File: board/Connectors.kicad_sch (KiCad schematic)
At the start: 20 parts, among them J10 SLOT 4, J11 SLOT 1, J12 SLOT 5, J13 SLOT 2, J14 SPI Device 0, J15 SPI Device 4, J16 SPI Device 1, J17 SPI Device 5, J19 SPI Device 2, J20 SPI Device 6, J21 SPI Device 3, J22 SPI Device 7, J23 SLOT 3, J24 VIA Port A, J25 SP720APP, J9 SLOT 0

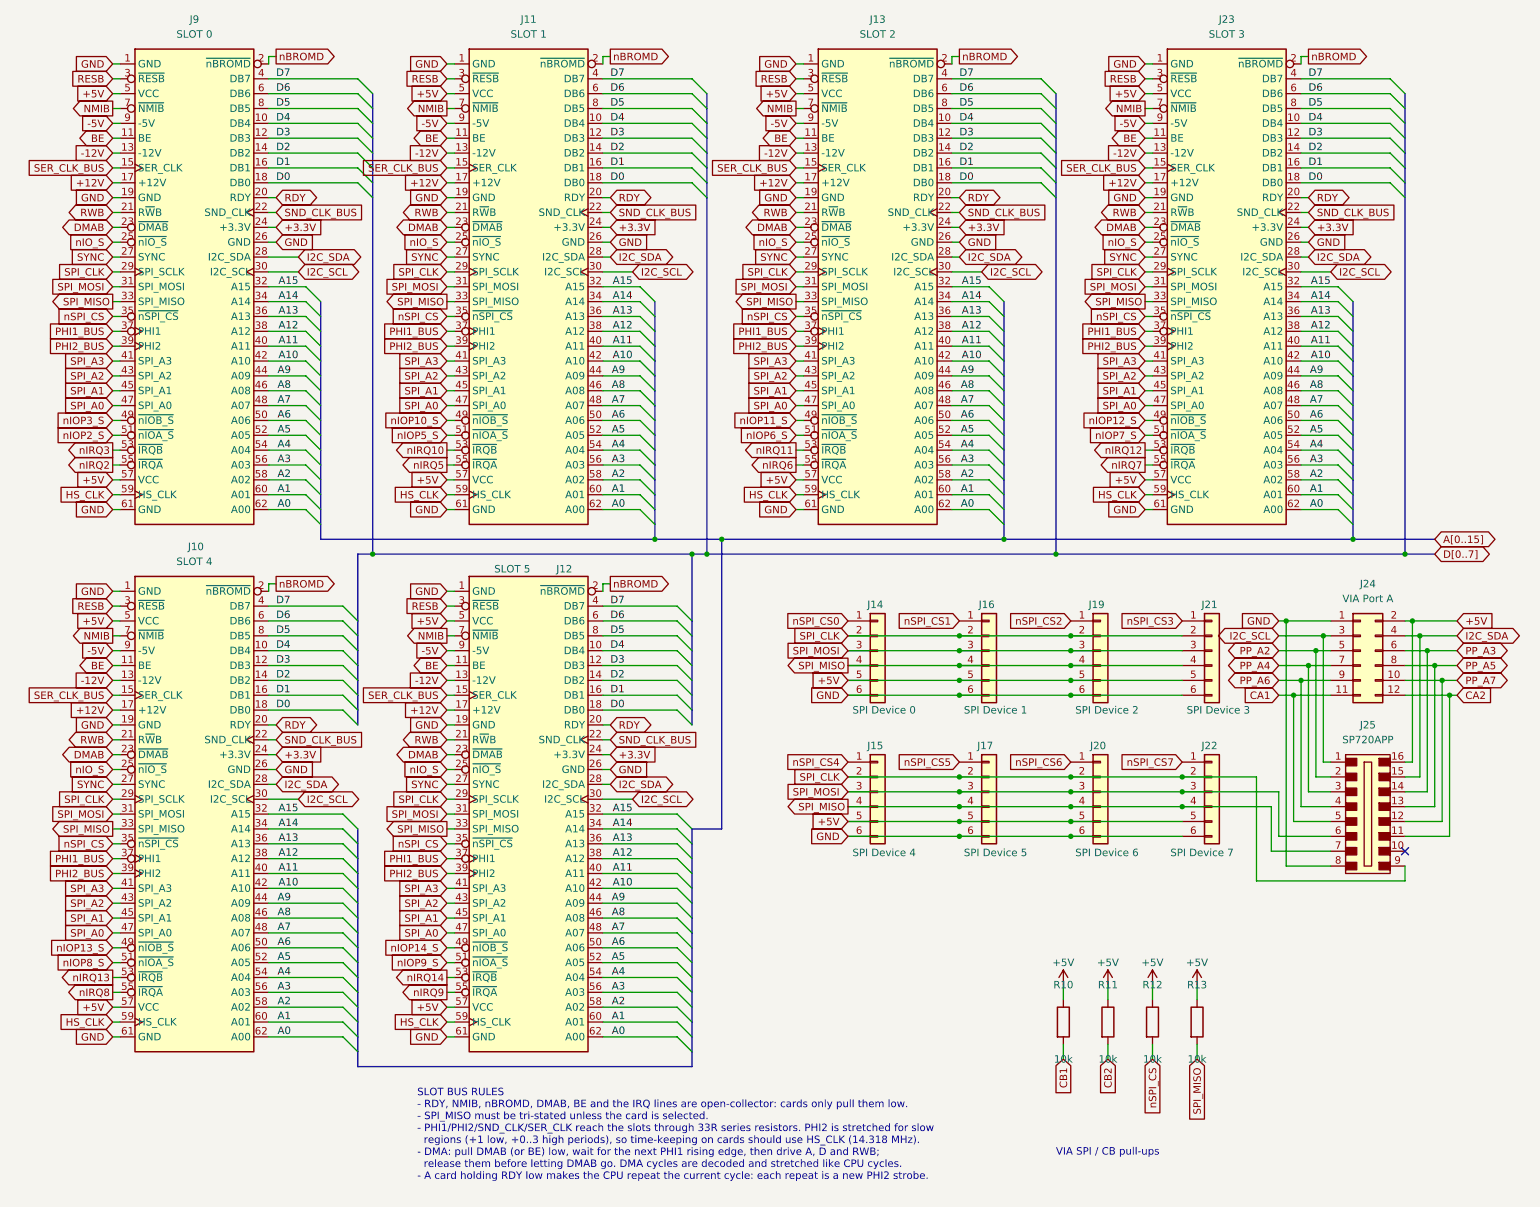
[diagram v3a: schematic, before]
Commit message: V2.0: slot pin 9 to +3.3V, amplifier on +5V
Slots:
- Pin 9 on all six slots now carries +3.3V instead of -5V, so each card
  gets two 3.3 V pins (9 and 24); no existing card used -5V
- Slot connector symbol pin 9 renamed +3.3V; slot bus rules note updated
- Removed U80 (79L05), C98 and C99 from the Power sheet

Amplifier:
- U89 TDA2822M now runs from +5V through an RC filter (R32 1R, C122 1000u)
- Removed U90 (L7809), C124 and C125
- R26/R27 470k (same volume range at 5 V); R30/R31 2.2R (same footprint)
- PWR_FLAG on the new AMP_5V net; sheet note updated

PCB updated from the schematic.

Also tidied overlapping text on the Power sheet (U78/U79 labels, PWR_FLAG,
R19/C111/R20/C112); connectivity unchanged.

Co-Authored-By: Claude Opus 5.5 <noreply@anthropic.com>
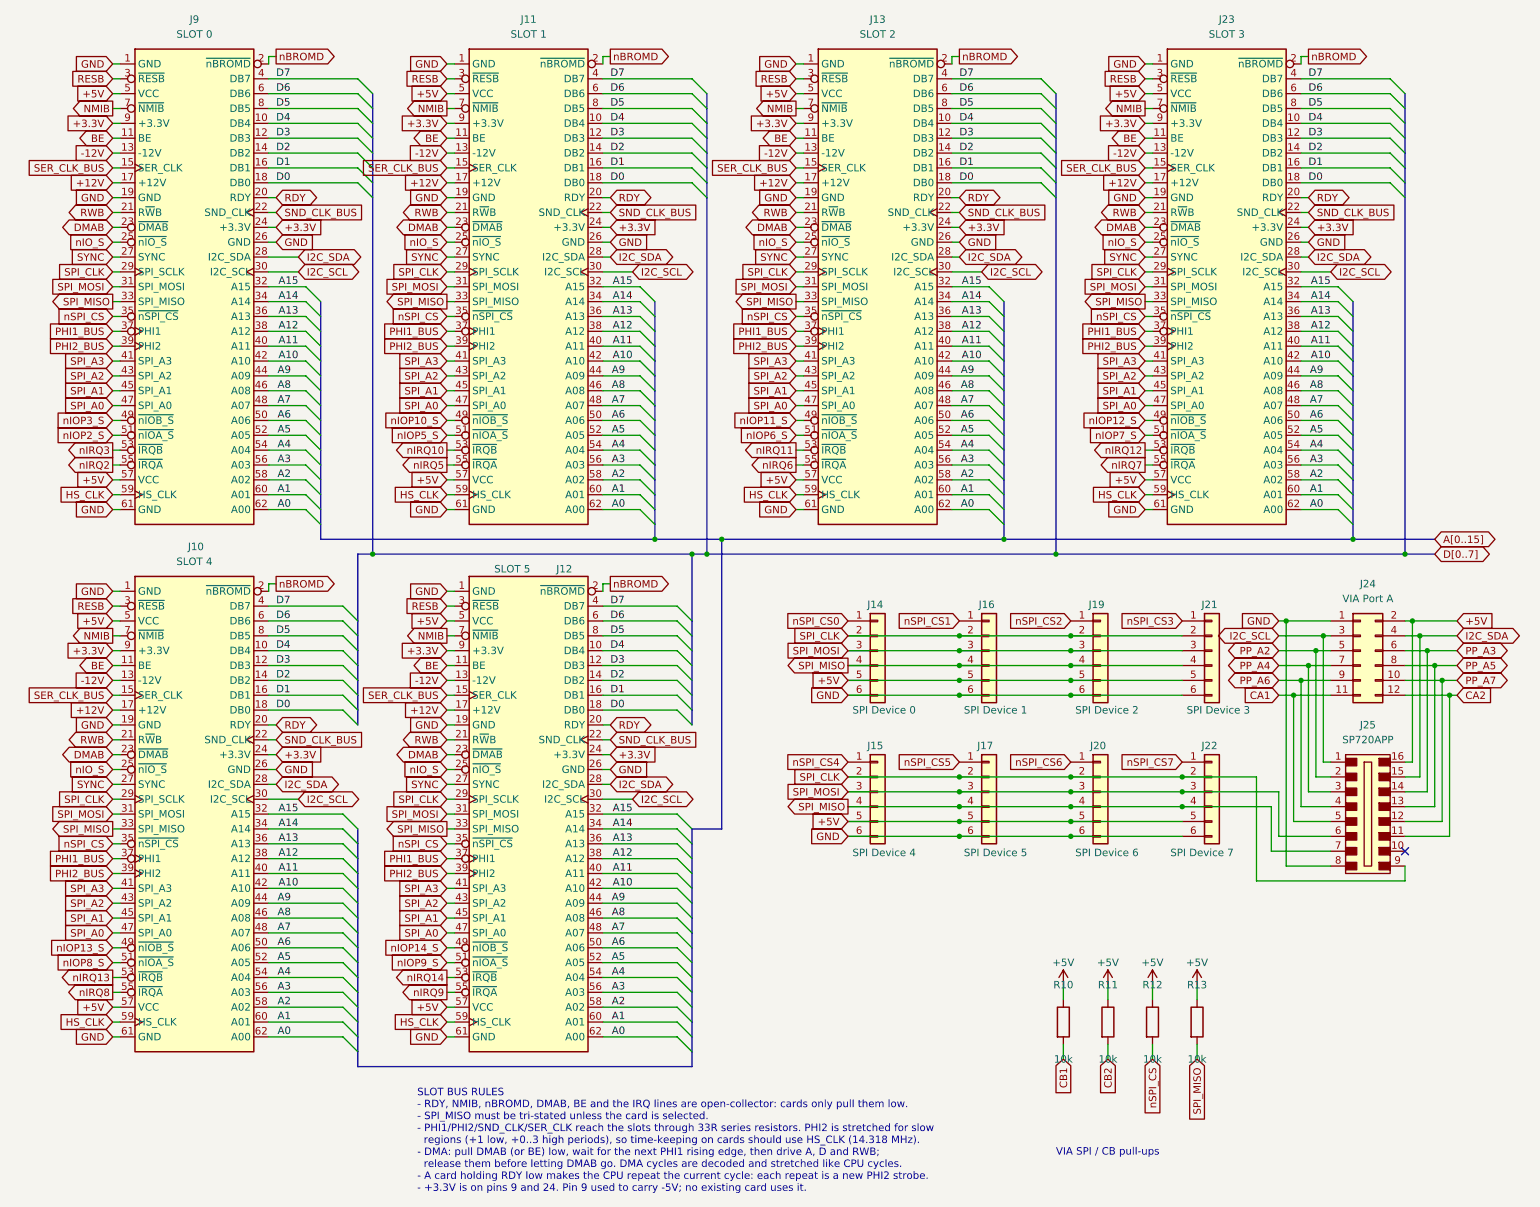
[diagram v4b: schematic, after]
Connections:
- net -5V is gone; now on net +3.3V: J10.9 (+3.3V), J11.9 (+3.3V), J12.9 (+3.3V), J13.9 (+3.3V), J23.9 (+3.3V), J9.9 (+3.3V)
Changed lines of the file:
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@@
 		(comment 1 "Hydra 16")
 	)
-	(text "SLOT BUS RULES\n- RDY, NMIB, nBROMD, DMAB, BE and the IRQ lines are open-collector: cards only pull them low.\n- SPI_MISO must be tri-stated unless the card is selected.\n- PHI1/PHI2/SND_CLK/SER_CLK reach the slots through 33R series resistors. PHI2 is stretched for slow\n  regions (+1 low, +0..3 high periods), so time-keeping on cards should use HS_CLK (14.318 MHz).\n- DMA: pull DMAB (or BE) low, wait for the next PHI1 rising edge, then drive A, D and RWB;\n  release them before letting DMAB go. DMA cycles are decoded and stretched like CPU cycles.\n- A card holding RDY low makes the CPU repeat the current cycle: each repeat is a new PHI2 strobe."
+	(text "SLOT BUS RULES\n- RDY, NMIB, nBROMD, DMAB, BE and the IRQ lines are open-collector: cards only pull them low.\n- SPI_MISO must be tri-stated unless the card is selected.\n- PHI1/PHI2/SND_CLK/SER_CLK reach the slots through 33R series resistors. PHI2 is stretched for slow\n  regions (+1 low, +0..3 high periods), so time-keeping on cards should use HS_CLK (14.318 MHz).\n- DMA: pull DMAB (or BE) low, wait for the next PHI1 rising edge, then drive A, D and RWB;\n  release them before letting DMAB go. DMA cycles are decoded and stretched like CPU cycles.\n- A card holding RDY low makes the CPU repeat the current cycle: each repeat is a new PHI2 strobe.\n- +3.3V is on pins 9 and 24. Pin 9 used to carry -5V; no existing card uses it."
 		(exclude_from_sim no)
 		(at 78.74 198.12 0)
@@
 		)
 	)
-	(global_label "-5V"
+	(global_label "+3.3V"
 		(shape input)
 		(at 143.51 33.02 180)
@@
 		)
 	)
-	(global_label "-5V"
+	(global_label "+3.3V"
 		(shape input)
 		(at 83.82 33.02 180)
@@
 		)
 	)
-	(global_label "-5V"
+	(global_label "+3.3V"
 		(shape input)
 		(at 26.67 123.19 180)
@@
 		)
 	)
-	(global_label "-5V"
+	(global_label "+3.3V"
 		(shape input)
 		(at 83.82 123.19 180)
@@
 		)
 	)
-	(global_label "-5V"
+	(global_label "+3.3V"
 		(shape input)
 		(at 26.67 33.02 180)
@@
 		)
 	)
-	(global_label "-5V"
+	(global_label "+3.3V"
 		(shape input)
 		(at 203.2 33.02 180)

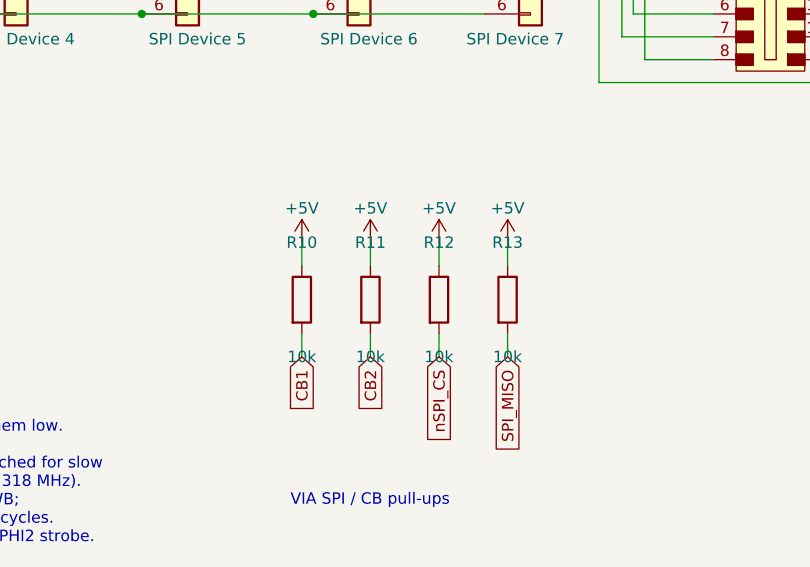
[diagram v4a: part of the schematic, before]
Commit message: V2.0: consolidate parts (239 -> 216), GAL C rev 02
No change in function:
- U9 74F08 removed: GAL C (U88) rev 02 makes the CPU phi0 (P_PHI0 = PHI2
  held low while DMAB_S is low); its decoupling cap C14 removed
- U34 74ACT14 removed: the two clock buffers use spare U19 74F240 gates
- U60 + U61 (2 x CY7C192 vector RAM) replaced by one AS7C256B-15
  (32K x 8, 15 ns); the IRQ sheet's D[0..7] bus is gone
- Crystal oscillators (U75 74HCU04, Y1, Y2, R1, R6-R8, C43, C44, C96,
  C97) replaced by canned oscillators X1 (14.31818 MHz), X2 (1.8432 MHz)
- Soft power: CD40106 -> 74HC14, CD4013 -> 74HC74 (active-low set/reset,
  power-on reset network inverted); a spare 74HC14 gate drives PS_ON#,
  so Q1 is removed
- R10-R13 -> RN6 (4 x 10k, SIP-5); R9, R21-R24 -> RN7 (5 x 33R isolated,
  SIP-10)
- C100-C102 (3 x 220u) -> C100 680u
- Clocks and Power sheet notes updated; PLD README updated

GAL C rev 02 verified against rev 01 over 200,000 clock edges.
PCB updated from the schematic (adds RN6, RN7, X1, X2 and the speakers
LS1/LS2). Also includes KiCad's re-save of the schematic sheets.

Co-Authored-By: Claude Opus 5.5 <noreply@anthropic.com>
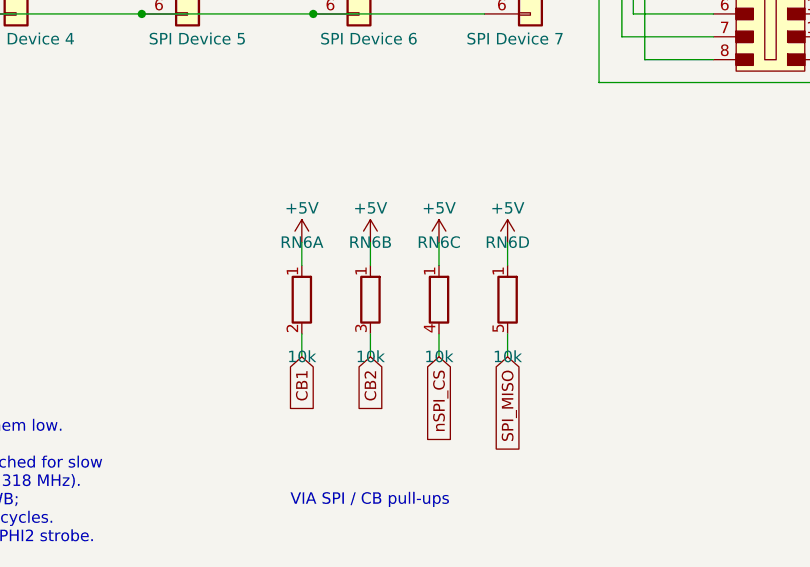
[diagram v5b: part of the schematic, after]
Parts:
- removed R11, R12, R13: 10k, Resistor_THT:R_Axial_DIN0204_L3.6mm_D1.6mm_P5.08mm_Horizontal, symbol Device:R
- added unit 2 of RN6
- added unit 3 of RN6
- added unit 4 of RN6
- RN6: renamed from R10; footprint Resistor_THT:R_Axial_DIN0204_L3.6mm_D1.6mm_P5.08mm_Horizontal -> Resistor_THT:R_Array_SIP5; symbol Device:R -> Device:R_Network04_Split
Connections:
- net +5V: now also RN6.1 (R1), RN6.1 (R1), RN6.1 (R1)
- net CB2: now also RN6.3 (R2.2)
- net SPI_MISO: now also RN6.5 (R4.2)
- net nSPI_CS: now also RN6.4 (R3.2)
